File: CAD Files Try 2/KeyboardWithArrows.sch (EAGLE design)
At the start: 168 parts

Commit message: Added wires to schematics. Need to wire to teensy pins
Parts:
- added _1: TEENSY, teensy:TEENSY
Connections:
- new net N$103: 4.P0, C.P0, F.P0, R.P0
- new net N$107: 3.P0, D.P0, E.P0, X.P0
- new net N$108: 2.P0, ALT.P0, S.P0, W.P0, Z.P0
- new net N$109: 1.P0, A.P0, Q.P0, WIN.P0
- new net N$110: CAPSLOCK.P0, CTRL.P0, ESC.P0, SHIFT.P0, TAB.P0
- new net N$111: KP_3.P0, KP_6.P0, KP_9.P0, NUMLOCK.P0
- new net N$112: KP_0.P0, KP_2.P0, KP_5.P0, KP_8.P0, KP_ASTERISK.P0
- new net N$113: KP_1.P0, KP_4.P0, KP_7.P0, KP_DEL.P0, KP_SLASH.P0
- new net N$114: ENTER2.P0, EQUAL2.P0, KP_DASH.P0
- new net N$72: DENTER2.A, ENTER2.P1
- new net N$73: DKP_DEL.A, KP_DEL.P1
- new net N$74: DKP_0.A, KP_0.P1
- new net N$75: CTRL.P1, DCTRL.A
- new net N$76: DWIN.A, WIN.P1
- new net N$77: ALT.P1, DALT.A
- new net N$78: DSPACE.A, SPACE.P1
- new net N$79: DFN.A, FN.P1
- new net N$80: CTRL2.P1, DCTRL2.A
- new net N$81: DLEFT.A, LEFT.P1
- new net N$82: DDOWN.A, DOWN.P1
- new net N$83: DRIGHT.A, RIGHT.P1
- new net N$84: F1.P0, F2.P0, F3.P0, F4.P0, RIGHT.P0
- new net N$85: CTRL2.P0, DASH.P0, LBRACKET.P0, QUOTE.P0, SLASH.P0
- new net N$86: BACKSLASH.P0, BACKSPACE.P0, DOWN.P0, ENTER.P0, UP.P0
- new net N$87: EQUAL.P0, LEFT.P0, RBRACKET.P0, SHIFT2.P0
- new net N$88: 0.P0, FN.P0, P.P0, PERIOD.P0, SEMICOLON.P0
- new net N$89: 9.P0, COMMA.P0, L.P0, O.P0
- new net N$92: 8.P0, I.P0, K.P0, M.P0
- new net N$93: 6.P0, B.P0, H.P0, SPACE.P0, Y.P0
- new net N$97: 7.P0, J.P0, N.P0, U.P0
- new net N$99: 5.P0, G.P0, T.P0, V.P0

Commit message: Added traces to board schematic
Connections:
- removed net N$103: 4.P0, C.P0, F.P0, R.P0
- removed net N$107: 3.P0, D.P0, E.P0, X.P0
- removed net N$108: 2.P0, ALT.P0, S.P0, W.P0, Z.P0
- removed net N$109: 1.P0, A.P0, Q.P0, WIN.P0
- removed net N$110: CAPSLOCK.P0, CTRL.P0, ESC.P0, SHIFT.P0, TAB.P0
- removed net N$111: KP_3.P0, KP_6.P0, KP_9.P0, NUMLOCK.P0
- removed net N$112: KP_0.P0, KP_2.P0, KP_5.P0, KP_8.P0, KP_ASTERISK.P0
- removed net N$113: KP_1.P0, KP_4.P0, KP_7.P0, KP_DEL.P0, KP_SLASH.P0
- removed net N$114: ENTER2.P0, EQUAL2.P0, KP_DASH.P0
- removed net N$84: F1.P0, F2.P0, F3.P0, F4.P0, RIGHT.P0
- removed net N$85: CTRL2.P0, DASH.P0, LBRACKET.P0, QUOTE.P0, SLASH.P0
- removed net N$86: BACKSLASH.P0, BACKSPACE.P0, DOWN.P0, ENTER.P0, UP.P0
- removed net N$87: EQUAL.P0, LEFT.P0, RBRACKET.P0, SHIFT2.P0
- removed net N$88: 0.P0, FN.P0, P.P0, PERIOD.P0, SEMICOLON.P0
- removed net N$89: 9.P0, COMMA.P0, L.P0, O.P0
- removed net N$92: 8.P0, I.P0, K.P0, M.P0
- removed net N$93: 6.P0, B.P0, H.P0, SPACE.P0, Y.P0
- removed net N$97: 7.P0, J.P0, N.P0, U.P0
- removed net N$99: 5.P0, G.P0, T.P0, V.P0
- removed net ROW1: D0.C, D1.C, D2.C, D3.C, D4.C, D5.C, D6.C, D7.C, D8.C, D9.C, DBACKSPACE.C, DDASH.C, DEQUAL.C, DESC.C, DF1.C, DKP_ASTERISK.C, DKP_DASH.C, DKP_SLASH.C, DNUMLOCK.C
- removed net ROW2: DBACKSLASH.C, DE.C, DEQUAL2.C, DF2.C, DI.C, DKP_7.C, DKP_8.C, DKP_9.C, DLBRACKET.C, DO.C, DP.C, DQ.C, DR.C, DRBRACKET.C, DT.C, DTAB.C, DU.C, DW.C, DY.C
- removed net ROW3: DA.C, DCAPSLOCK.C, DD.C, DENTER.C, DF.C, DF3.C, DG.C, DH.C, DJ.C, DK.C, DKP_4.C, DKP_5.C, DKP_6.C, DL.C, DQUOTE.C, DS.C, DSEMICOLON.C
- removed net ROW4: DB.C, DC.C, DCOMMA.C, DENTER2.C, DF4.C, DKP_1.C, DKP_2.C, DKP_3.C, DM.C, DN.C, DPERIOD.C, DSHIFT.C, DSHIFT2.C, DSLASH.C, DUP.C, DV.C, DX.C, DZ.C
- removed net ROW5: DALT.C, DCTRL.C, DCTRL2.C, DDOWN.C, DFN.C, DKP_0.C, DKP_DEL.C, DLEFT.C, DRIGHT.C, DSPACE.C, DWIN.C
- new net PINB0: EQUAL.P0, LEFT.P0, RBRACKET.P0, SHIFT2.P0, _1._B0
- new net PINB1: CTRL2.P0, DASH.P0, LBRACKET.P0, QUOTE.P0, SLASH.P0, _1._B1
- new net PINB2: 0.P0, FN.P0, P.P0, PERIOD.P0, SEMICOLON.P0, _1._B2
- new net PINB3: 9.P0, COMMA.P0, L.P0, O.P0, _1._B3
- new net PINB4: 8.P0, I.P0, K.P0, M.P0, _1._B4
- new net PINB5: 7.P0, J.P0, N.P0, U.P0, _1._B5
- new net PINB6: 6.P0, B.P0, H.P0, SPACE.P0, Y.P0, _1._B6
- new net PINB7: 5.P0, G.P0, T.P0, V.P0, _1._B7
- new net PINC6: KP_0.P0, KP_2.P0, KP_5.P0, KP_8.P0, KP_ASTERISK.P0, _1._C6
- new net PINC7: KP_1.P0, KP_4.P0, KP_7.P0, KP_DEL.P0, KP_SLASH.P0, _1._C7
- new net PIND0: D0.C, D1.C, D2.C, D3.C, D4.C, D5.C, D6.C, D7.C, D8.C, D9.C, DBACKSPACE.C, DDASH.C, DEQUAL.C, DESC.C, DF1.C, DKP_ASTERISK.C, DKP_DASH.C, DKP_SLASH.C, DNUMLOCK.C, _1._D0
- new net PIND1: DBACKSLASH.C, DE.C, DEQUAL2.C, DF2.C, DI.C, DKP_7.C, DKP_8.C, DKP_9.C, DLBRACKET.C, DO.C, DP.C, DQ.C, DR.C, DRBRACKET.C, DT.C, DTAB.C, DU.C, DW.C, DY.C, _1._D1
- new net PIND2: DA.C, DCAPSLOCK.C, DD.C, DENTER.C, DF.C, DF3.C, DG.C, DH.C, DJ.C, DK.C, DKP_4.C, DKP_5.C, DKP_6.C, DL.C, DQUOTE.C, DS.C, DSEMICOLON.C, _1._D2
- new net PIND3: DB.C, DC.C, DCOMMA.C, DENTER2.C, DF4.C, DKP_1.C, DKP_2.C, DKP_3.C, DM.C, DN.C, DPERIOD.C, DSHIFT.C, DSHIFT2.C, DSLASH.C, DUP.C, DV.C, DX.C, DZ.C, _1._D3
- new net PIND4: DALT.C, DCTRL.C, DCTRL2.C, DDOWN.C, DFN.C, DKP_0.C, DKP_DEL.C, DLEFT.C, DRIGHT.C, DSPACE.C, DWIN.C, _1._D4
- new net PIND5: F1.P0, F2.P0, F3.P0, F4.P0, RIGHT.P0, _1._D5
- new net PIND7: BACKSLASH.P0, BACKSPACE.P0, DOWN.P0, ENTER.P0, UP.P0, _1._D7
- new net PINE6: ENTER2.P0, EQUAL2.P0, KP_DASH.P0, _1._E6
- new net PINF0: 4.P0, C.P0, F.P0, R.P0, _1._F0
- new net PINF1: 3.P0, D.P0, E.P0, X.P0, _1._F1
- new net PINF4: 2.P0, ALT.P0, S.P0, W.P0, Z.P0, _1._F4
- new net PINF5: 1.P0, A.P0, Q.P0, WIN.P0, _1._F5
- new net PINF6: CAPSLOCK.P0, CTRL.P0, ESC.P0, SHIFT.P0, TAB.P0, _1._F6
- new net PINF7: KP_3.P0, KP_6.P0, KP_9.P0, NUMLOCK.P0, _1._F7

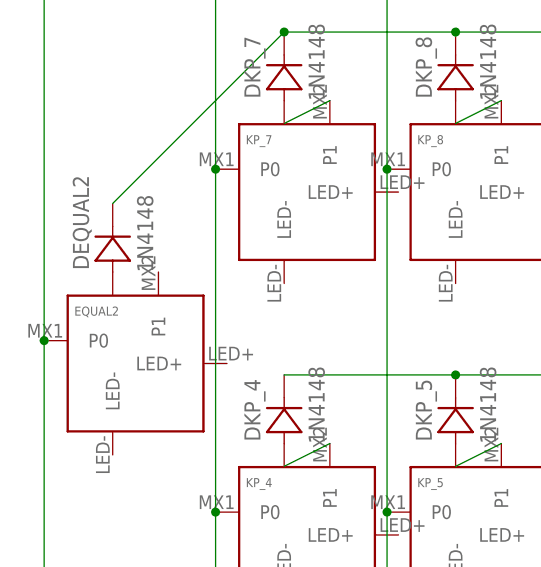
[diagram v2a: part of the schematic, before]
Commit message: Fixed part of board where a key was missing a connection
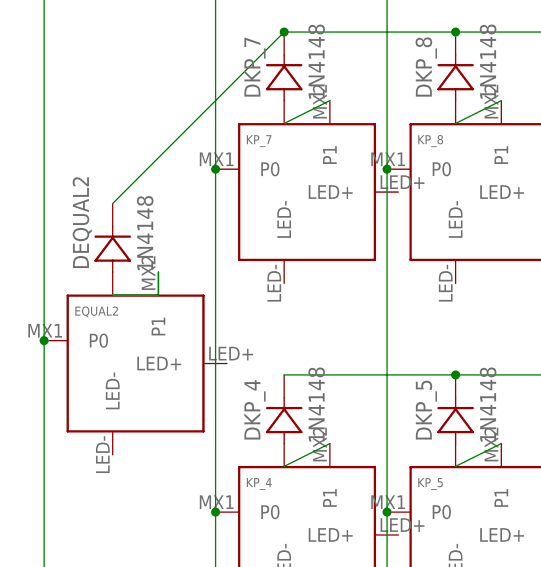
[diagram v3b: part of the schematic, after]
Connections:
- new net N$84: DEQUAL2.A, EQUAL2.P1
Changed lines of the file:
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@@
+</segment>
+</net>
+<net name="N$84" class="0">
+<segment>
+<pinref part="EQUAL2" gate="G$1" pin="P1"/>
+<pinref part="DEQUAL2" gate="D$1" pin="A"/>
+<wire x1="11.938" y1="-66.04" x2="11.938" y2="-68.58" width="0.1524" layer="91"/>
+<wire x1="11.938" y1="-68.58" x2="6.858" y2="-68.58" width="0.1524" layer="91"/>
 </segment>
 </net>
